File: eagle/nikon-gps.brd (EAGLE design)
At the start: 29.5 x 29.5 mm, 12 parts, among them IC1 GPS-A2235-H, IC2 LP2985SOT, IC3 MAX3370, P1 TPTP12SQ, P2 TPTP12SQ, P3 TPTP12SQ

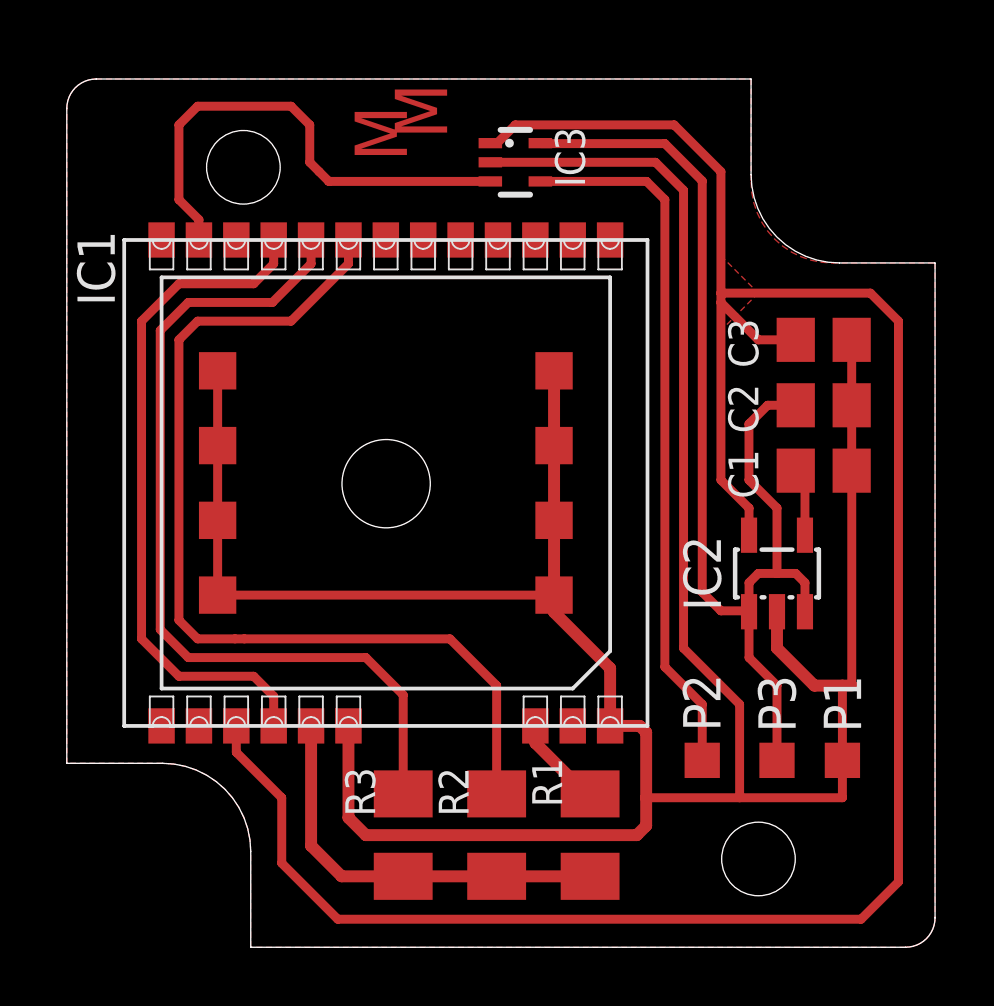
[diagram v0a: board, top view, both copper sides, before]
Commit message: Updating PCB to fit inside the lid (now 28.5mm x 28.5mm).
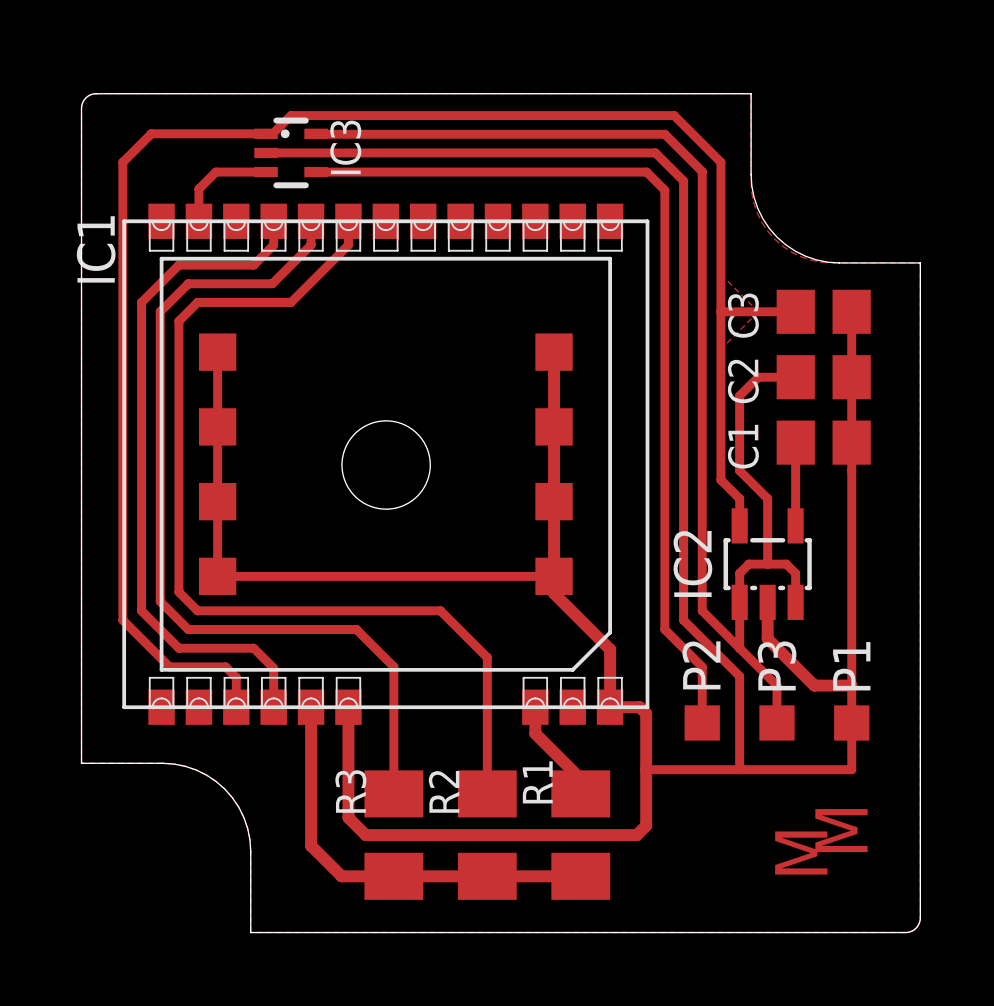
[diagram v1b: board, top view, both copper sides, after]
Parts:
- moved IC3 7.63 mm to (7.62, 27.0)
- moved P1 1.31 mm to (26.7, 7.62)
- moved P2 1.27 mm to (21.6, 7.62)
- moved P3 1.27 mm to (24.1, 7.62)
- moved C1 0.95 mm to (25.7, 17.1)
- moved C2 0.95 mm to (25.7, 19.4)
- moved C3 0.95 mm to (25.7, 21.6)
- moved IC1 0.63 mm to (4.49, 12.0)
- moved IC2 0.45 mm to (23.8, 13.0)
- moved R1 0.32 mm to (17.5, 3.81)
- moved R2 0.32 mm to (14.3, 3.81)
- moved R3 0.32 mm to (11.1, 3.81)
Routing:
- net +3V3: track 77.6 -> 58.0 mm
- net N$2: track 16.8 -> 3.62 mm
- net GND: track 105.1 -> 114.2 mm
- net +5V: track 38.8 -> 47.5 mm
- net N$3: track 24.1 -> 30.7 mm
- net N$1: track 2.32 -> 2.83 mm
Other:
- board size 29.5 x 29.5 mm -> 28.5 x 28.5 mm
